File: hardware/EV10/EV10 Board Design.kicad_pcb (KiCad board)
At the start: 4 copper layers, 72.7 x 89.4 mm, 112 parts, among them J11 Conn_01x06_Female, J12 Conn_01x04_Female, J13 Conn_01x04_Female, J2 Conn_01x02_Female, J3 Conn_01x02_Socket, J4 Conn_01x08_Male, J5 Conn_01x02_Socket, J6 Conn_01x04_Female, J7 Conn_01x04_Female, J8 Conn_01x06_Female, J9 USB_C_Receptacle, SW4 SW_Push, SW5 SW_Push, U1 STM32F405RGTx, U11 ESP32-S3-WROOM-1-N8R2, U13 BM14B(0.8)-24DS-0.4V(53), U2 MCP73832-2-OT, U3 CH340C, U4 USBLC6-2P6, U5 STM32F030C8Tx, U6 WM8960CGEFL/RV, U7 TPS63060, Y1 Crystal_GND24

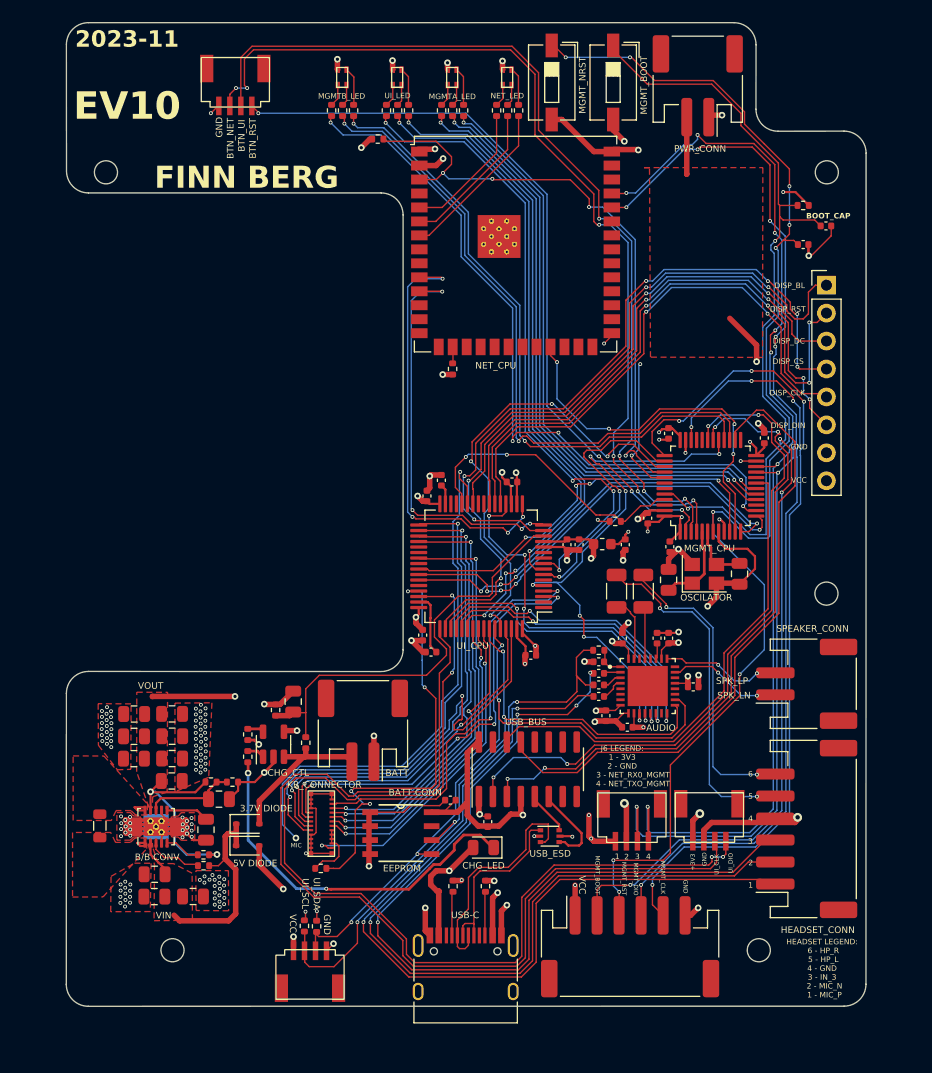
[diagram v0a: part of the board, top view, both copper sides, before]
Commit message: EV10 Design with new screen connector and pwr mgmt
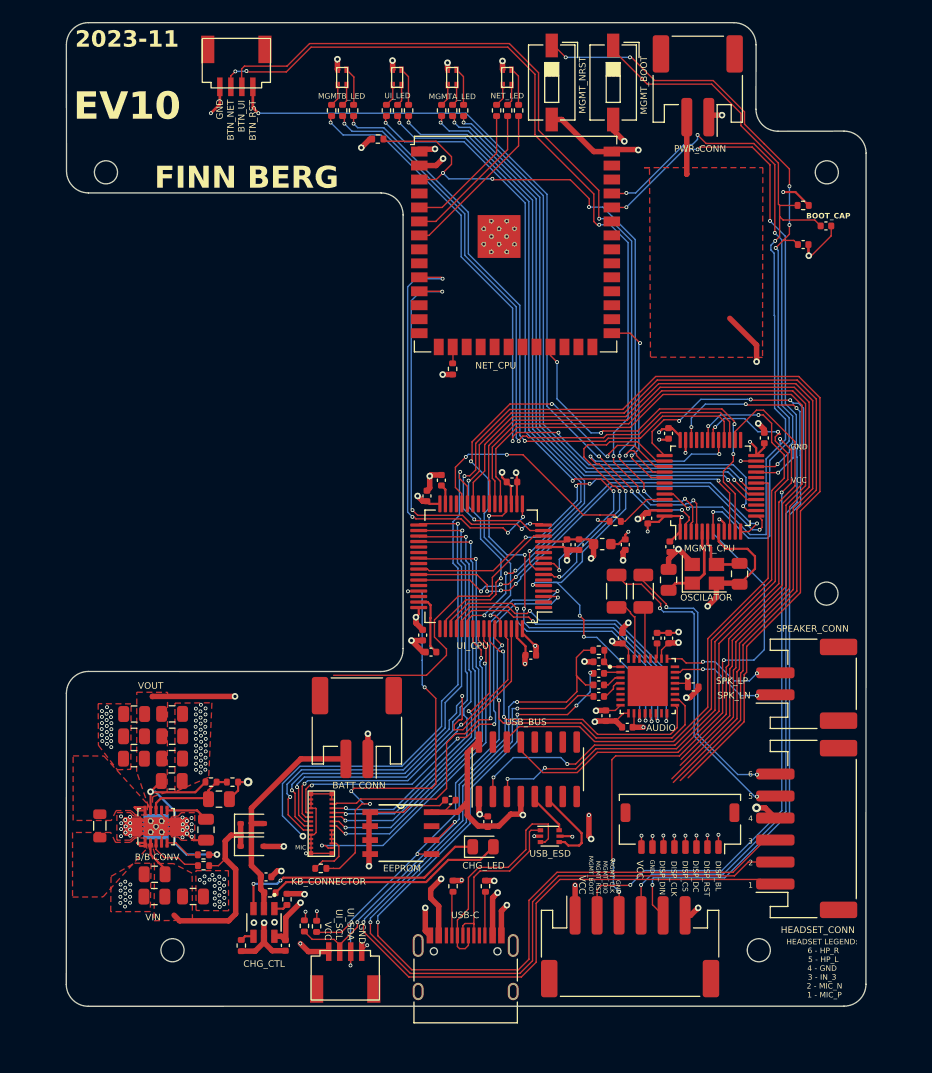
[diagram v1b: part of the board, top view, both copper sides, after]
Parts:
- removed J12, J6: Conn_01x04_Female, 1x4 pin download:1x4pin 1mm connector
- removed J3: Conn_01x02_Socket, Connector_JST:JST_PH_S2B-PH-SM4-TB_1x02-1MP_P2.00mm_Horizontal
- removed J4: Conn_01x08_Male, Connector_PinHeader_2.54mm:PinHeader_1x08_P2.54mm_Vertical
- removed R28, R29: 10k, Resistor_SMD:R_0402_1005Metric
- added C2: 10u, Capacitor_SMD:C_0402_1005Metric, F.Cu at (132.1, 133.7)
- added J1: Conn_01x02_Socket, Connector_JST:JST_PH_S2B-PH-SM4-TB_1x02-1MP_P2.00mm_Horizontal, F.Cu at (140.4, 120.1)
- added J10: Conn_01x08_Socket, Connector_JST:JST_SHL_SM08B-SHLS-TF_1x08-1MP_P1.00mm_Horizontal, F.Cu at (169.8, 129.3)
- added R22: 10k, Resistor_SMD:R_0402_1005Metric, F.Cu at (134.0, 135.7)
- C1: value 4.7u -> 10u; footprint Capacitor_SMD:C_0805_2012Metric -> Capacitor_SMD:C_0402_1005Metric
- R26: value 1k -> 680
- R27: value 1k -> 1k5
- U2: value MCP73832-2-OT -> BQ21040DBVR; footprint Package_TO_SOT_SMD:SOT-23-5 -> BQ21040DBVR:SOT95P280X145-6N
- moved C1 22.2 mm to (133.9, 139.9), turned to -90 degrees
- moved R26 19.2 mm to (129.9, 139.9), turned to -90 degrees
- moved U2 16.2 mm to (131.9, 137.8), turned to -90 degrees
- moved R27 12.5 mm to (132.5, 135.1), turned to 0 degrees
- moved J7 3.20 mm to (136.7, 143.9)
- moved J13 1.74 mm to (132.0, 58.5)
- moved D6 0.41 mm to (130.9, 130.9)
- moved D2 0.40 mm to (130.9, 128.8)
- moved D1 0.08 mm to (151.9, 130.9), turned to 0 degrees
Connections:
- net /UI_RX1_NET renamed /UI_RX2_NET
- net /UI_TX1_NET renamed /UI_TX2_NET
- C1 pad 1: /BATTERY_MON -> VBUS
- D1 pad 2: VBUS -> Net-(D1-A)
- R26 pad 1: GND -> Net-(U2-ISET)
- R26 pad 2: Net-(U2-PROG) -> GND
- R27 pad 1: Net-(D1-K) -> Net-(D2-A)
- R27 pad 2: Net-(U2-STAT) -> Net-(D1-A)
- U1 pad 46: /UI_SWDIO -> unconnected-(U1-PA13-Pad46)
- U1 pad 49: /UI_SWDCLK -> unconnected-(U1-PA14-Pad49)
- U2 pad 1: Net-(U2-STAT) -> Net-(U2-TS)
- U2 pad 2: GND -> Net-(D2-A)
- U2 pad 3: Net-(D2-A) -> Net-(D1-K)
- U2 pad 4: VBUS -> Net-(U2-ISET)
- U2 pad 5: Net-(U2-PROG) -> GND
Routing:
- net /UI_SWDIO: track 97.2 -> 0.00 mm, vias 4 -> 0
- net /UI_SWDCLK: track 91.4 -> 0.00 mm
- net /NET_RX1_MGMT: track 100.0 -> 49.0 mm, vias 7 -> 4
- net /NET_TX1_MGMT: track 99.1 -> 48.9 mm, vias 7 -> 4
- net /DISP_DC: track 49.0 -> 79.6 mm, vias 2 -> 1
- net /DISP_BL: track 66.6 -> 96.5 mm, vias 4 -> 3
- net /DISP_CS: track 62.6 -> 89.9 mm, vias 6 -> 3
- net /DISP_SPI_MOSI: track 54.0 -> 77.7 mm, vias 4 -> 1
- net /DISP_SPI_SCK: track 50.0 -> 73.3 mm, vias 2 -> 1
- net Net-(D1-A): track 0.00 -> 21.5 mm
- net /DISP_RSTR: track 56.2 -> 75.0 mm, vias 4 -> 1
- net GND: track 577.3 -> 560.1 mm, vias 151 -> 154
- net VBUS: track 70.2 -> 55.9 mm
- net Net-(D1-K): track 34.1 -> 23.6 mm
- net /BATTERY_MON: track 38.9 -> 28.6 mm
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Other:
- outline, holes or cut-outs redrawn
- board text removed: "+3V3"
- board text removed: "3.7V DIODE"
- board text removed: "5V DIODE"
- board text removed: "BATT"
- board text removed: "J6 LEGEND: 1 - 3V3 2 - GND 3 - NET_RX0_MGMT 4 - NET_TXO_MGMT"
- board text removed: "UI_CLK"
- board text removed: "UI_DIO"

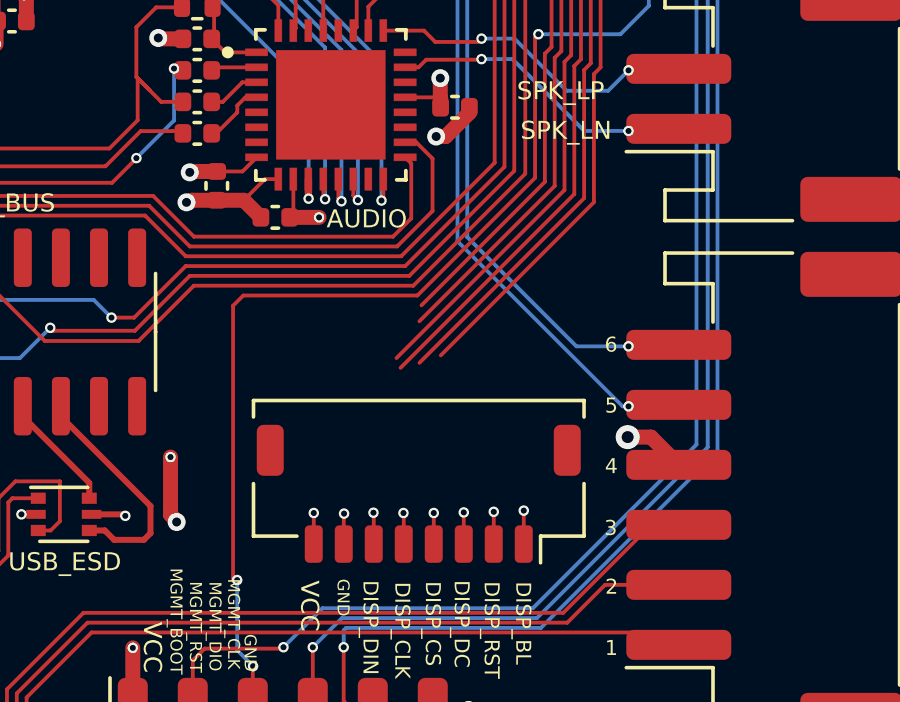
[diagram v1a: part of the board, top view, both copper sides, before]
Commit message: EV10 bord design with V2 pwr mgmt and screen conn
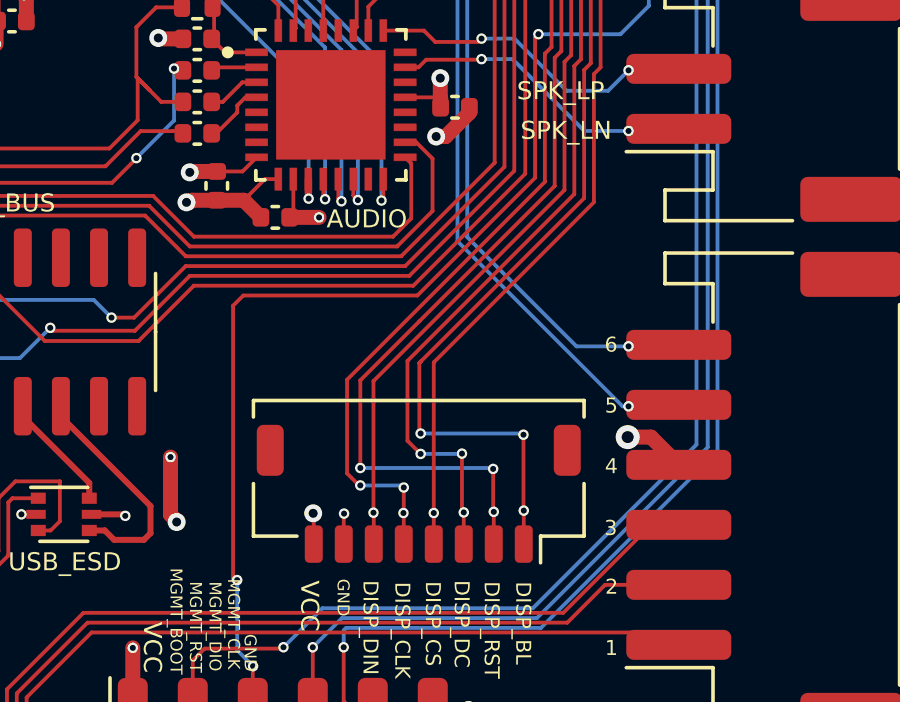
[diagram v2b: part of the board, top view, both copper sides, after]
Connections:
- J10 pad 8: /VIN -> +3.3V
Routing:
- net /DISP_RSTR: track 75.0 -> 86.6 mm, vias 1 -> 3
- net /DISP_SPI_SCK: track 73.3 -> 82.8 mm, vias 1 -> 3
- net /DISP_BL: track 96.5 -> 104.9 mm, vias 3 -> 5
- net GND: track 560.1 -> 566.8 mm
- net /DISP_DC: track 79.6 -> 85.9 mm, vias 1 -> 3
- net +3.3V: track 452.4 -> 458.1 mm, vias 27 -> 28
- net /DISP_SPI_MOSI: track 77.7 -> 83.2 mm
- net /DISP_CS: track 89.9 -> 95.3 mm
- net /VIN: track 1.03 -> 0.00 mm, vias 1 -> 0
